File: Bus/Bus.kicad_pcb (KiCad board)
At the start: 2 copper layers, 80 x 93.2 mm, 27 parts, among them J1 Clock, J12 Instruction Register, J13 A Register, J17 A Register, J18 MAR, J19 MAR, J2 Control Logic Flags #1, J20 B Register, J25 B Register, J26 Memory, J29 Memory, J3 Output Register, J30 Arithmetic Logic Unit, J31 Arithmetic Logic Unit, J32 Program Counter, J36 Program Counter, J5 Output Register, J8 Instruction Register, J9 Control Logic Flags #2

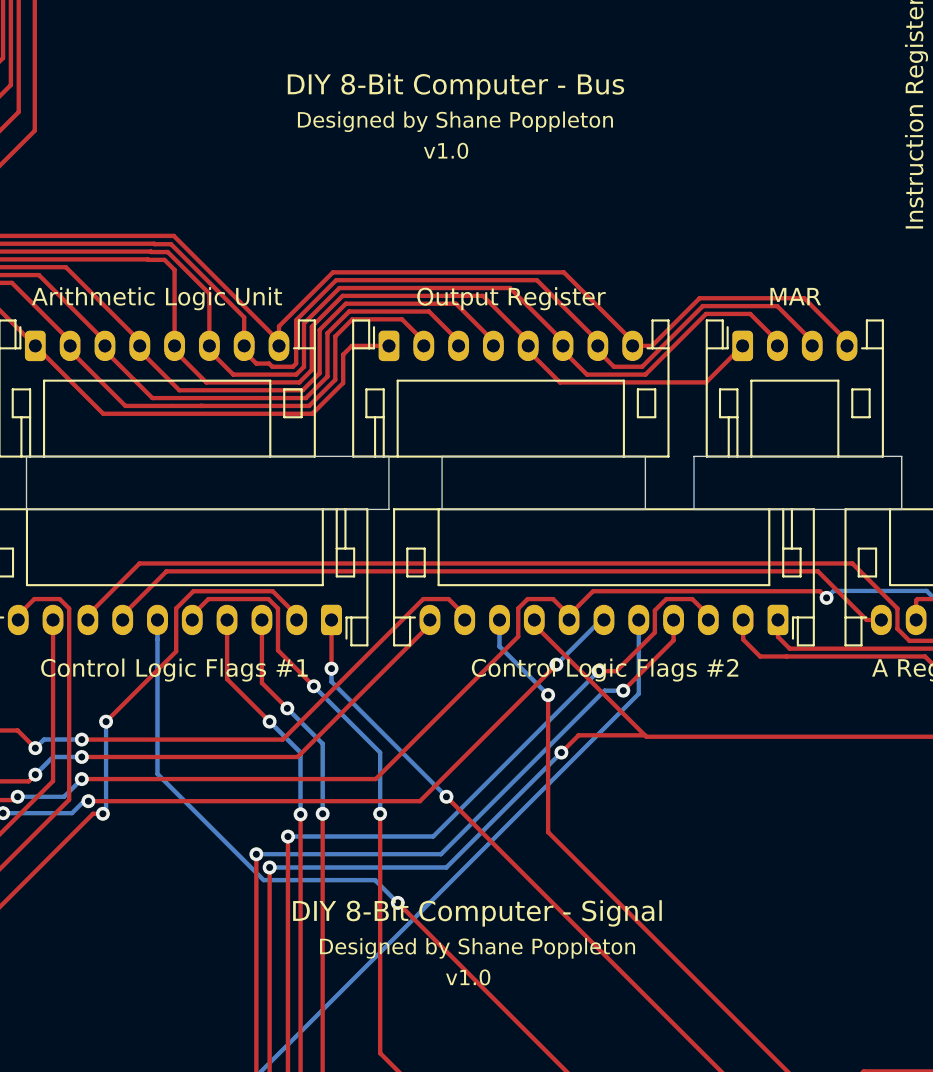
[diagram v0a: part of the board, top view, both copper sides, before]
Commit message: Added Attribution on each PCB, and regenerated gerbers
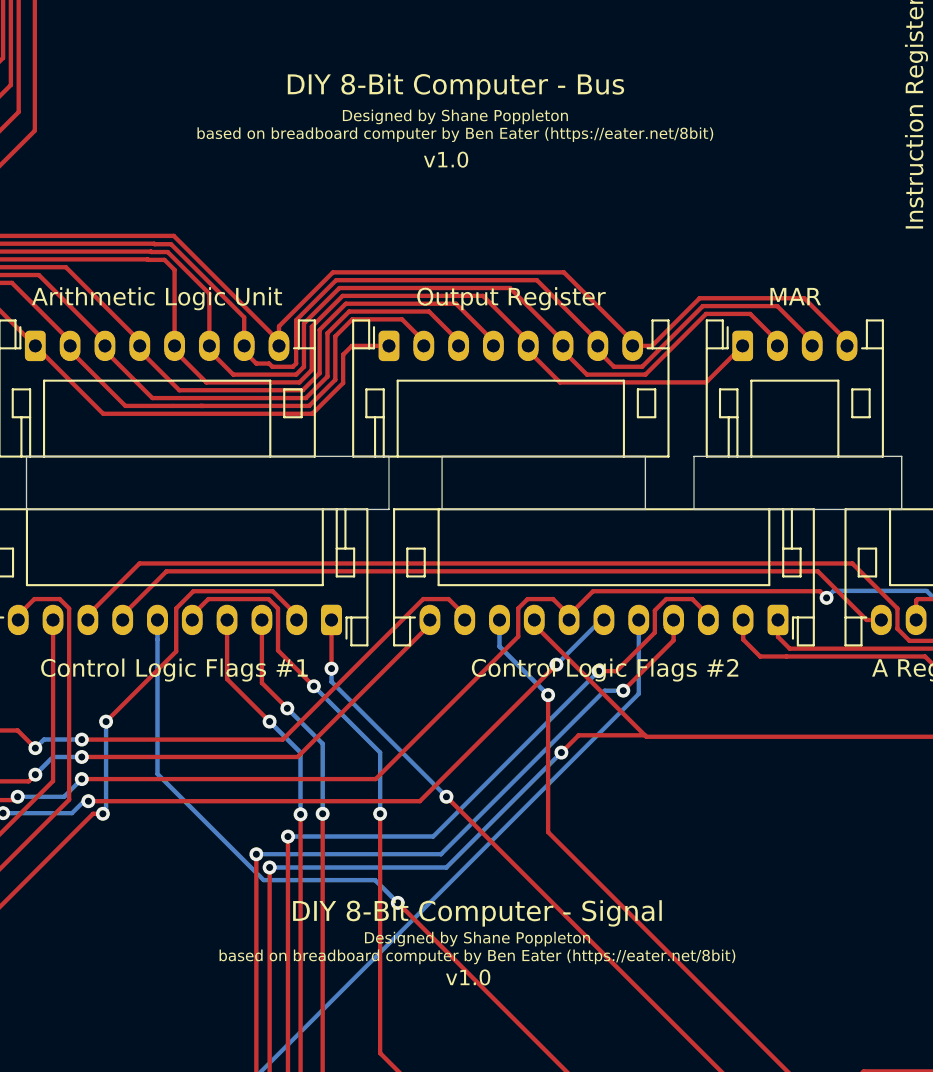
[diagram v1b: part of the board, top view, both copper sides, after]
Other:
- board text added: "Designed by Shane Poppleton based on breadboard computer by Ben Eater (https://eater.net/8bit)"
- board text removed: "Designed by Shane Poppleton"
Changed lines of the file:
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@@
     )
   )
-  (gr_text "Designed by Shane Poppleton" (at 133.858 110.998) (layer F.SilkS)
-    (effects (font (size 0.889 0.889) (thickness 0.127)))
+  (gr_text "Designed by Shane Poppleton\nbased on breadboard computer by Ben Eater (https://eater.net/8bit)\n" (at 133.858 110.998) (layer F.SilkS)
+    (effects (font (size 0.635 0.635) (thickness 0.1016)))
   )
   (gr_text v1.0 (at 133.35 112.776) (layer F.SilkS)
@@
   (gr_arc (start 171.958 89.662) (end 175.768 89.662) (angle -90) (layer Edge.Cuts) (width 0.05))
   (gr_arc (start 99.568 89.662) (end 99.568 85.852) (angle -90) (layer Edge.Cuts) (width 0.05))
-  (gr_text v1.0 (at 132.08 65.278) (layer F.SilkS)
+  (gr_text v1.0 (at 132.08 65.786) (layer F.SilkS)
     (effects (font (size 0.889 0.889) (thickness 0.127)))
   )
-  (gr_text "Designed by Shane Poppleton" (at 132.588 63.5) (layer F.SilkS)
-    (effects (font (size 0.889 0.889) (thickness 0.127)))
+  (gr_text "Designed by Shane Poppleton\nbased on breadboard computer by Ben Eater (https://eater.net/8bit)\n" (at 132.588 63.754) (layer F.SilkS)
+    (effects (font (size 0.635 0.635) (thickness 0.1016)))
   )
   (gr_text "DIY 8-Bit Computer - Bus" (at 132.588 61.468) (layer F.SilkS)
